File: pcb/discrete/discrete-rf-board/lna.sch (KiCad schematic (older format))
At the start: 7 parts, among them J701 Conn_Coaxial, J702 Conn_Coaxial, J703 Conn_Coaxial, J704 Conn_Coaxial, U701 SF2098H

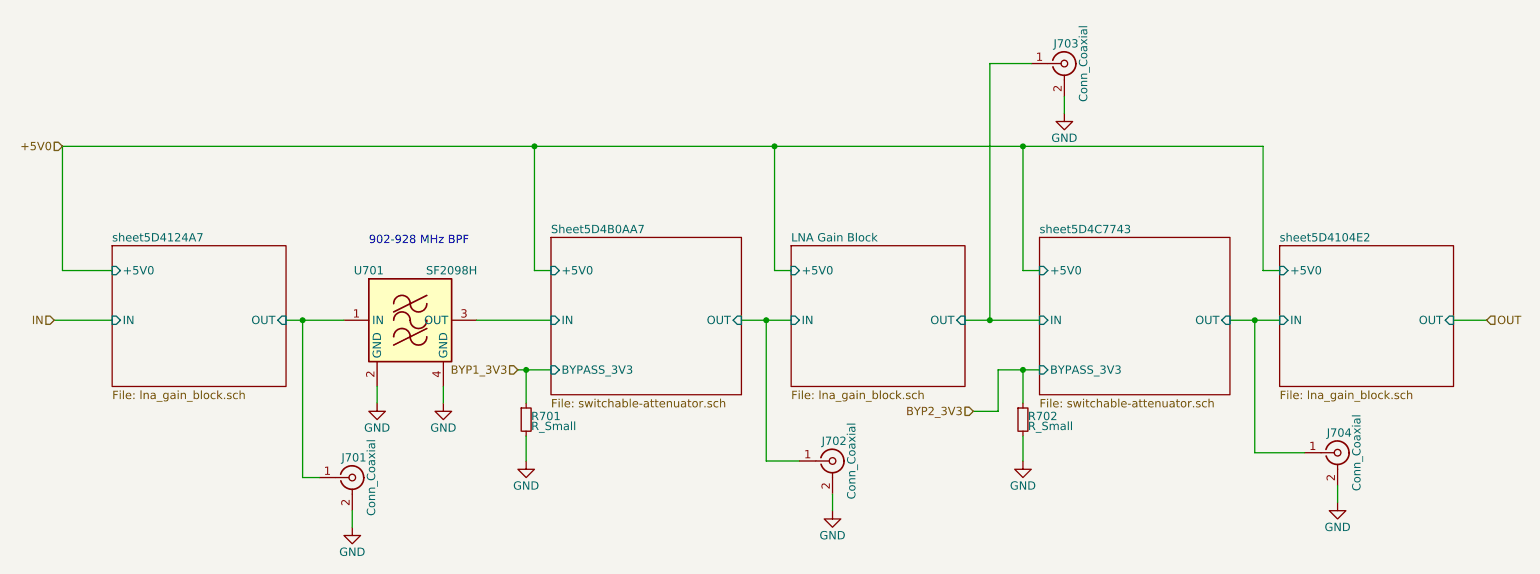
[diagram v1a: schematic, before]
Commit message: Wire out all control signals to connectors TODO PLL charge pump loop, bypass caps in attenuator circuit, antialiasing filter for ADC frontend
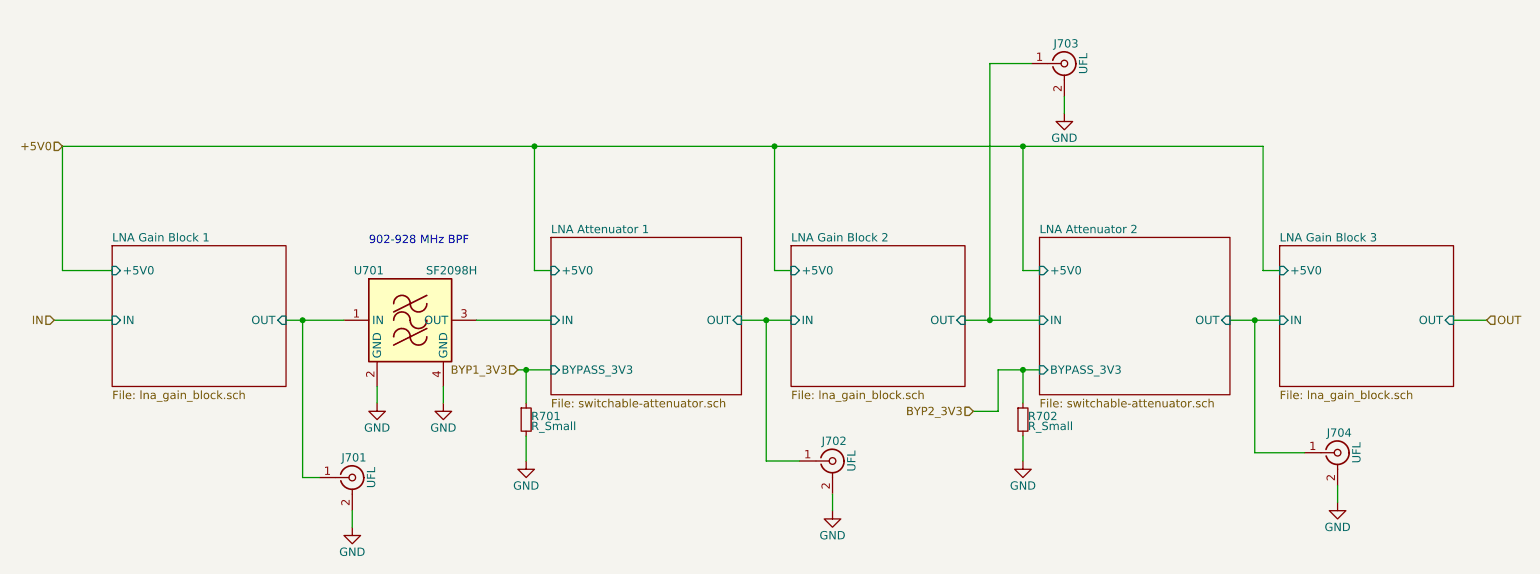
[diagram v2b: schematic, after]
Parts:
- J701, J702, J703, J704: value Conn_Coaxial -> UFL
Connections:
- net LNA Gain Block/IN renamed LNA Attenuator 1/OUT
- net LNA Gain Block/OUT renamed LNA Attenuator 2/IN
- net Sheet5D4B0AA7/IN renamed LNA Attenuator 1/IN
- net sheet5D4104E2/IN renamed LNA Attenuator 2/OUT
- net sheet5D4124A7/OUT renamed LNA Gain Block 1/OUT
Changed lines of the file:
@@
 $Descr A4 11693 8268
 encoding utf-8
-Sheet 6 19
+Sheet 13 19
 Title ""
 Date ""
@@
 S 5500 3200 1050 850
 U 5D3C8D48
-F0 "LNA Gain Block" 50
+F0 "LNA Gain Block 2" 50
 F1 "lna_gain_block.sch" 50
 F2 "IN" I L 5500 3650 50
@@
 S 8450 3200 1050 850
 U 5D4104E7
-F0 "sheet5D4104E2" 50
+F0 "LNA Gain Block 3" 50
 F1 "lna_gain_block.sch" 50
 F2 "IN" I L 8450 3650 50
@@
 S 1400 3200 1050 850
 U 5D4124AC
-F0 "sheet5D4124A7" 50
+F0 "LNA Gain Block 1" 50
 F1 "lna_gain_block.sch" 50
 F2 "IN" I L 1400 3650 50
@@
 S 4050 3150 1150 950
 U 5D4B0AA8
-F0 "Sheet5D4B0AA7" 50
+F0 "LNA Attenuator 1" 50
 F1 "switchable-attenuator.sch" 50
 F2 "OUT" I R 5200 3650 50
@@
 S 7000 3150 1150 950
 U 5D4C7749
-F0 "sheet5D4C7743" 50
+F0 "LNA Attenuator 2" 50
 F1 "switchable-attenuator.sch" 50
 F2 "OUT" I R 8150 3650 50
@@
 P 2850 4600
 F 0 "J701" H 2860 4720 50  0000 C CNN
-F 1 "Conn_Coaxial" V 2965 4600 50  0000 C CNN
+F 1 "UFL" V 2965 4600 50  0000 C CNN
 F 2 "" H 2850 4600 50  0001 C CNN
 F 3 " ~" H 2850 4600 50  0001 C CNN
@@
 P 5750 4500
 F 0 "J702" H 5760 4620 50  0000 C CNN
-F 1 "Conn_Coaxial" V 5865 4500 50  0000 C CNN
+F 1 "UFL" V 5865 4500 50  0000 C CNN
 F 2 "" H 5750 4500 50  0001 C CNN
 F 3 " ~" H 5750 4500 50  0001 C CNN
@@
 P 8800 4450
 F 0 "J704" H 8810 4570 50  0000 C CNN
-F 1 "Conn_Coaxial" V 8915 4450 50  0000 C CNN
+F 1 "UFL" V 8915 4450 50  0000 C CNN
 F 2 "" H 8800 4450 50  0001 C CNN
 F 3 " ~" H 8800 4450 50  0001 C CNN
@@
 P 7150 2100
 F 0 "J703" H 7160 2220 50  0000 C CNN
-F 1 "Conn_Coaxial" V 7265 2100 50  0000 C CNN
+F 1 "UFL" V 7265 2100 50  0000 C CNN
 F 2 "" H 7150 2100 50  0001 C CNN
 F 3 " ~" H 7150 2100 50  0001 C CNN

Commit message: Fix some parts
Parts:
- U701: footprint (none) -> discrete_footprints:Murata_SM2016-4; Mouser (none) -> 719-SF2098H
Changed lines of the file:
@@
 F 0 "U701" H 2950 3950 50  0000 C CNN
 F 1 "SF2098H" H 3450 3950 50  0000 C CNN
-F 2 "" H 3200 3200 50  0001 C CNN
+F 2 "discrete_footprints:Murata_SM2016-4" H 3200 3200 50  0001 C CNN
 F 3 "" H 3200 4050 50  0001 C CNN
+F 4 " 719-SF2098H " H 3200 3650 50  0001 C CNN "Mouser"
 	1    3200 3650
 	1    0    0    -1

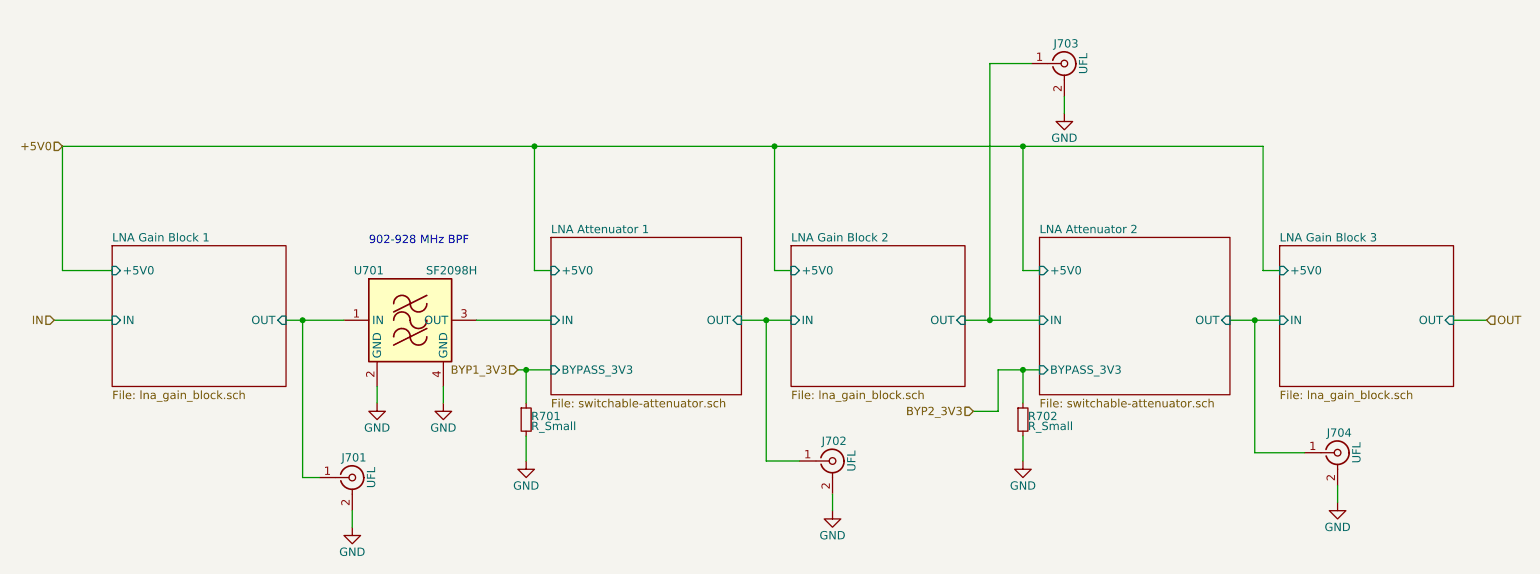
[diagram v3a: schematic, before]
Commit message: Add matching PNP/NPN transistor pairs, fix pin numbering for BFU520R transistors TODO fix biasing on power stage, source last NPN transistor, autofill and start sourcing passives
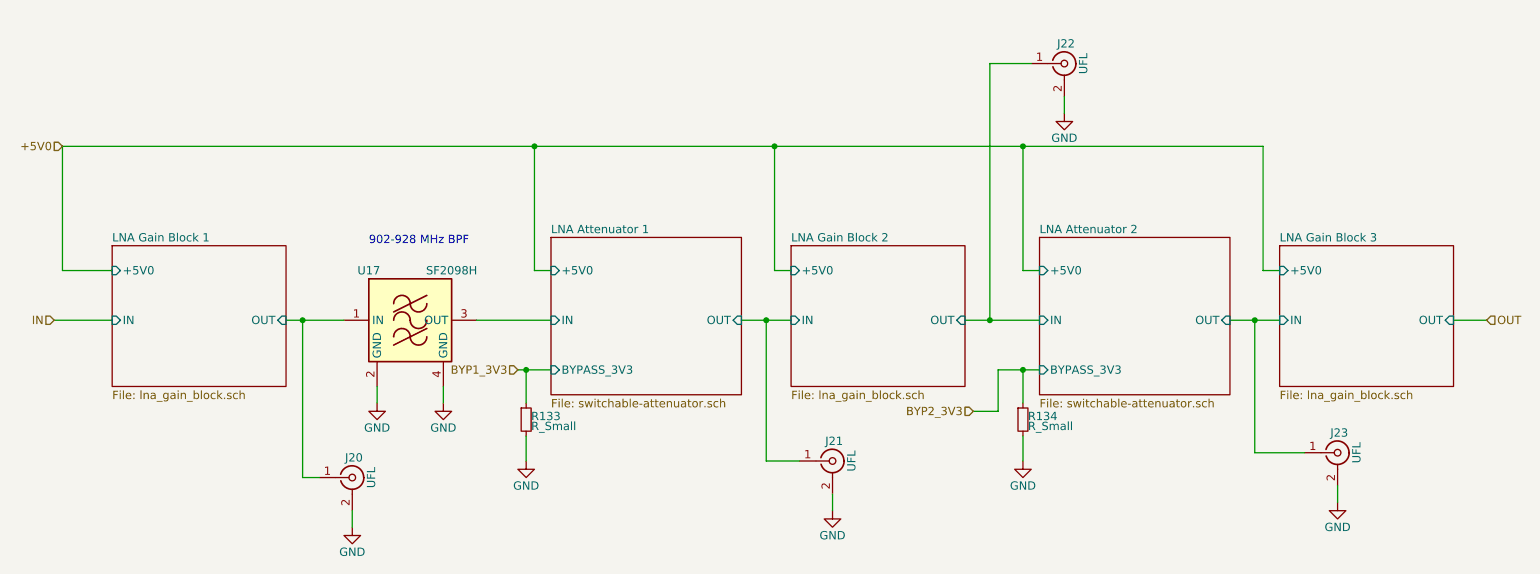
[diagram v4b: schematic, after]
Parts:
- renumbered J701 to J20, J702 to J21, J703 to J22, J704 to J23, R701 to R133, R702 to R134, U701 to U17
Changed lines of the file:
@@
 Connection ~ 6900 2600
 $Comp
-L discrete-parts:SF2098H U701
+L discrete-parts:SF2098H U17
 U 1 1 5D1AD426
 P 3200 3650
-F 0 "U701" H 2950 3950 50  0000 C CNN
+F 0 "U17" H 2950 3950 50  0000 C CNN
 F 1 "SF2098H" H 3450 3950 50  0000 C CNN
 F 2 "discrete_footprints:Murata_SM2016-4" H 3200 3200 50  0001 C CNN
@@
 	2450 3650 2550 3650
 $Comp
-L power:GND #PWR0702
+L power:GND #PWR0192
 U 1 1 5D1AE626
 P 3000 4150
-F 0 "#PWR0702" H 3000 3900 50  0001 C CNN
+F 0 "#PWR0192" H 3000 3900 50  0001 C CNN
 F 1 "GND" H 3000 4000 50  0000 C CNN
 F 2 "" H 3000 4150 50  0001 C CNN
@@
 $EndComp
 $Comp
-L power:GND #PWR0703
+L power:GND #PWR0193
 U 1 1 5D1AE8E4
 P 3400 4150
-F 0 "#PWR0703" H 3400 3900 50  0001 C CNN
+F 0 "#PWR0193" H 3400 3900 50  0001 C CNN
 F 1 "GND" H 3400 4000 50  0000 C CNN
 F 2 "" H 3400 4150 50  0001 C CNN
@@
 902-928 MHz BPF
 $Comp
-L Device:R_Small R701
+L Device:R_Small R133
 U 1 1 5D1B2D1C
 P 3900 4250
-F 0 "R701" H 3930 4270 50  0000 L CNN
+F 0 "R133" H 3930 4270 50  0000 L CNN
 F 1 "R_Small" H 3930 4210 50  0000 L CNN
 F 2 "" H 3900 4250 50  0001 C CNN
@@
 $EndComp
 $Comp
-L Device:R_Small R702
+L Device:R_Small R134
 U 1 1 5D1B32F5
 P 6900 4250
-F 0 "R702" H 6930 4270 50  0000 L CNN
+F 0 "R134" H 6930 4270 50  0000 L CNN
 F 1 "R_Small" H 6930 4210 50  0000 L CNN
 F 2 "" H 6900 4250 50  0001 C CNN
@@
 	3900 3950 4050 3950
 $Comp
-L power:GND #PWR0704
+L power:GND #PWR0194
 U 1 1 5D1B4BA9
 P 3900 4500
-F 0 "#PWR0704" H 3900 4250 50  0001 C CNN
+F 0 "#PWR0194" H 3900 4250 50  0001 C CNN
 F 1 "GND" H 3900 4350 50  0000 C CNN
 F 2 "" H 3900 4500 50  0001 C CNN
@@
 	6900 3950 7000 3950
 $Comp
-L power:GND #PWR0706
+L power:GND #PWR0196
 U 1 1 5D1B5E5F
 P 6900 4500
-F 0 "#PWR0706" H 6900 4250 50  0001 C CNN
+F 0 "#PWR0196" H 6900 4250 50  0001 C CNN
 F 1 "GND" H 6900 4350 50  0000 C CNN
 F 2 "" H 6900 4500 50  0001 C CNN
@@
 	6900 4500 6900 4350
 $Comp
-L Connector:Conn_Coaxial J701
+L Connector:Conn_Coaxial J20
 U 1 1 5D1BAD0A
 P 2850 4600
-F 0 "J701" H 2860 4720 50  0000 C CNN
+F 0 "J20" H 2860 4720 50  0000 C CNN
 F 1 "UFL" V 2965 4600 50  0000 C CNN
 F 2 "" H 2850 4600 50  0001 C CNN
@@
 $EndComp
 $Comp
-L Connector:Conn_Coaxial J702
+L Connector:Conn_Coaxial J21
 U 1 1 5D1BB7C4
 P 5750 4500
-F 0 "J702" H 5760 4620 50  0000 C CNN
+F 0 "J21" H 5760 4620 50  0000 C CNN
 F 1 "UFL" V 5865 4500 50  0000 C CNN
 F 2 "" H 5750 4500 50  0001 C CNN
@@
 $EndComp
 $Comp
-L Connector:Conn_Coaxial J704
+L Connector:Conn_Coaxial J23
 U 1 1 5D1BC003
 P 8800 4450
-F 0 "J704" H 8810 4570 50  0000 C CNN
+F 0 "J23" H 8810 4570 50  0000 C CNN
 F 1 "UFL" V 8915 4450 50  0000 C CNN
 F 2 "" H 8800 4450 50  0001 C CNN
@@
 $EndComp
 $Comp
-L Connector:Conn_Coaxial J703
+L Connector:Conn_Coaxial J22
 U 1 1 5D1BCC67
 P 7150 2100
-F 0 "J703" H 7160 2220 50  0000 C CNN
+F 0 "J22" H 7160 2220 50  0000 C CNN
 F 1 "UFL" V 7265 2100 50  0000 C CNN
 F 2 "" H 7150 2100 50  0001 C CNN
@@
 $EndComp
 $Comp
-L power:GND #PWR0707
+L power:GND #PWR0197
 U 1 1 5D1BD3CE
 P 7150 2400
-F 0 "#PWR0707" H 7150 2150 50  0001 C CNN
+F 0 "#PWR0197" H 7150 2150 50  0001 C CNN
 F 1 "GND" H 7150 2250 50  0000 C CNN
 F 2 "" H 7150 2400 50  0001 C CNN
@@
 $EndComp
 $Comp
-L power:GND #PWR0708
+L power:GND #PWR0198
 U 1 1 5D1BDEF3
 P 8800 4750
-F 0 "#PWR0708" H 8800 4500 50  0001 C CNN
+F 0 "#PWR0198" H 8800 4500 50  0001 C CNN
 F 1 "GND" H 8800 4600 50  0000 C CNN
 F 2 "" H 8800 4750 50  0001 C CNN
@@
 $EndComp
 $Comp
-L power:GND #PWR0705
+L power:GND #PWR0195
 U 1 1 5D1BE3A6
 P 5750 4800
-F 0 "#PWR0705" H 5750 4550 50  0001 C CNN
+F 0 "#PWR0195" H 5750 4550 50  0001 C CNN
 F 1 "GND" H 5750 4650 50  0000 C CNN
 F 2 "" H 5750 4800 50  0001 C CNN
@@
 $EndComp
 $Comp
-L power:GND #PWR0701
+L power:GND #PWR0191
 U 1 1 5D1BE863
 P 2850 4900
-F 0 "#PWR0701" H 2850 4650 50  0001 C CNN
+F 0 "#PWR0191" H 2850 4650 50  0001 C CNN
 F 1 "GND" H 2850 4750 50  0000 C CNN
 F 2 "" H 2850 4900 50  0001 C CNN

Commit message: Autofill all; TODO improve formatting on autofill_all output
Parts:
- J20, J21, J22, J23: footprint (none) -> discrete_footprints:2337019-1; Mouser (none) -> 571-2337019-1
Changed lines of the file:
@@
 F 0 "J20" H 2860 4720 50  0000 C CNN
 F 1 "UFL" V 2965 4600 50  0000 C CNN
-F 2 "" H 2850 4600 50  0001 C CNN
+F 2 "discrete_footprints:2337019-1" H 2850 4600 50  0001 C CNN
 F 3 " ~" H 2850 4600 50  0001 C CNN
+F 4 " 571-2337019-1" H 2850 4600 50  0001 C CNN "Mouser"
 	1    2850 4600
 	1    0    0    -1
@@
 F 0 "J21" H 5760 4620 50  0000 C CNN
 F 1 "UFL" V 5865 4500 50  0000 C CNN
-F 2 "" H 5750 4500 50  0001 C CNN
+F 2 "discrete_footprints:2337019-1" H 5750 4500 50  0001 C CNN
 F 3 " ~" H 5750 4500 50  0001 C CNN
+F 4 " 571-2337019-1" H 5750 4500 50  0001 C CNN "Mouser"
 	1    5750 4500
 	1    0    0    -1
@@
 F 0 "J23" H 8810 4570 50  0000 C CNN
 F 1 "UFL" V 8915 4450 50  0000 C CNN
-F 2 "" H 8800 4450 50  0001 C CNN
+F 2 "discrete_footprints:2337019-1" H 8800 4450 50  0001 C CNN
 F 3 " ~" H 8800 4450 50  0001 C CNN
+F 4 " 571-2337019-1" H 8800 4450 50  0001 C CNN "Mouser"
 	1    8800 4450
 	1    0    0    -1
@@
 F 0 "J22" H 7160 2220 50  0000 C CNN
 F 1 "UFL" V 7265 2100 50  0000 C CNN
-F 2 "" H 7150 2100 50  0001 C CNN
+F 2 "discrete_footprints:2337019-1" H 7150 2100 50  0001 C CNN
 F 3 " ~" H 7150 2100 50  0001 C CNN
+F 4 " 571-2337019-1" H 7150 2100 50  0001 C CNN "Mouser"
 	1    7150 2100
 	1    0    0    -1

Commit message: Footprint some stuff
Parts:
- R133, R134: value R_Small -> 10kR
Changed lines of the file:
@@
 P 3900 4250
 F 0 "R133" H 3930 4270 50  0000 L CNN
-F 1 "R_Small" H 3930 4210 50  0000 L CNN
+F 1 "10kR" H 3930 4210 50  0000 L CNN
 F 2 "" H 3900 4250 50  0001 C CNN
 F 3 "~" H 3900 4250 50  0001 C CNN
@@
 P 6900 4250
 F 0 "R134" H 6930 4270 50  0000 L CNN
-F 1 "R_Small" H 6930 4210 50  0000 L CNN
+F 1 "10kR" H 6930 4210 50  0000 L CNN
 F 2 "" H 6900 4250 50  0001 C CNN
 F 3 "~" H 6900 4250 50  0001 C CNN

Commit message: Autofill
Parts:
- R133, R134: footprint (none) -> Resistor_SMD:R_0402_1005Metric; Mouser (none) -> 603-AC0402FR-1310KL
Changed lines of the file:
@@
 F 0 "R133" H 3930 4270 50  0000 L CNN
 F 1 "10kR" H 3930 4210 50  0000 L CNN
-F 2 "" H 3900 4250 50  0001 C CNN
+F 2 "Resistor_SMD:R_0402_1005Metric" H 3900 4250 50  0001 C CNN
 F 3 "~" H 3900 4250 50  0001 C CNN
+F 4 "603-AC0402FR-1310KL" H 3900 4250 50  0001 C CNN "Mouser"
 	1    3900 4250
 	1    0    0    -1
@@
 F 0 "R134" H 6930 4270 50  0000 L CNN
 F 1 "10kR" H 6930 4210 50  0000 L CNN
-F 2 "" H 6900 4250 50  0001 C CNN
+F 2 "Resistor_SMD:R_0402_1005Metric" H 6900 4250 50  0001 C CNN
 F 3 "~" H 6900 4250 50  0001 C CNN
+F 4 "603-AC0402FR-1310KL" H 6900 4250 50  0001 C CNN "Mouser"
 	1    6900 4250
 	1    0    0    -1

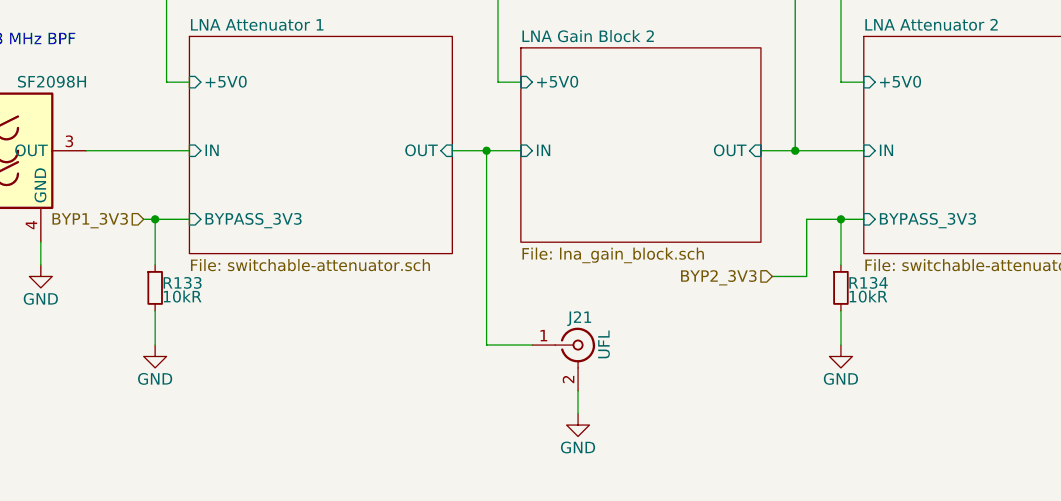
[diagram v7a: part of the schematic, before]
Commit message: Reannotate everything; I'm trying to cut down the number of components
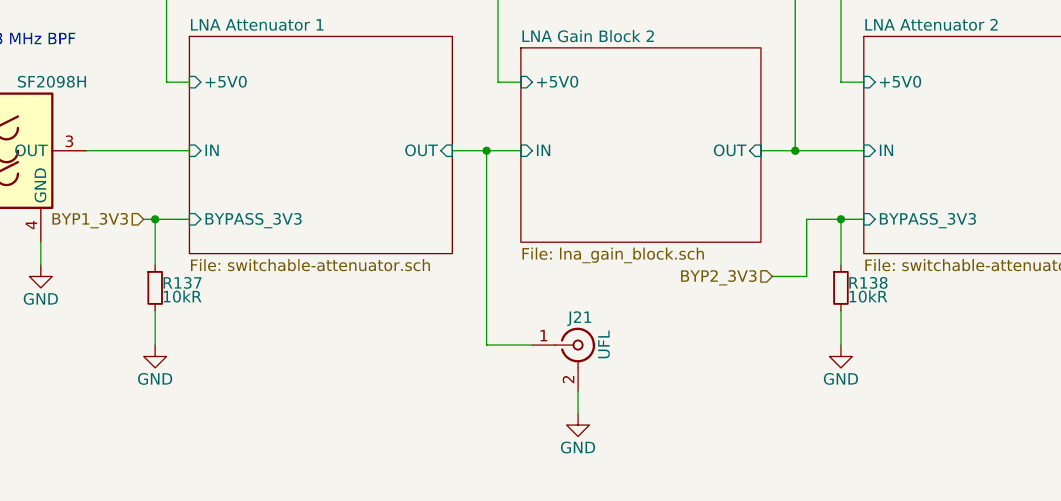
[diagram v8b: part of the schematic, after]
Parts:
- renumbered R133 to R137, R134 to R138
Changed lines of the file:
@@
 	2450 3650 2550 3650
 $Comp
-L power:GND #PWR0192
+L power:GND #PWR0189
 U 1 1 5D1AE626
 P 3000 4150
-F 0 "#PWR0192" H 3000 3900 50  0001 C CNN
+F 0 "#PWR0189" H 3000 3900 50  0001 C CNN
 F 1 "GND" H 3000 4000 50  0000 C CNN
 F 2 "" H 3000 4150 50  0001 C CNN
@@
 $EndComp
 $Comp
-L power:GND #PWR0193
+L power:GND #PWR0190
 U 1 1 5D1AE8E4
 P 3400 4150
-F 0 "#PWR0193" H 3400 3900 50  0001 C CNN
+F 0 "#PWR0190" H 3400 3900 50  0001 C CNN
 F 1 "GND" H 3400 4000 50  0000 C CNN
 F 2 "" H 3400 4150 50  0001 C CNN
@@
 902-928 MHz BPF
 $Comp
-L Device:R_Small R133
+L Device:R_Small R137
 U 1 1 5D1B2D1C
 P 3900 4250
-F 0 "R133" H 3930 4270 50  0000 L CNN
+F 0 "R137" H 3930 4270 50  0000 L CNN
 F 1 "10kR" H 3930 4210 50  0000 L CNN
 F 2 "Resistor_SMD:R_0402_1005Metric" H 3900 4250 50  0001 C CNN
@@
 $EndComp
 $Comp
-L Device:R_Small R134
+L Device:R_Small R138
 U 1 1 5D1B32F5
 P 6900 4250
-F 0 "R134" H 6930 4270 50  0000 L CNN
+F 0 "R138" H 6930 4270 50  0000 L CNN
 F 1 "10kR" H 6930 4210 50  0000 L CNN
 F 2 "Resistor_SMD:R_0402_1005Metric" H 6900 4250 50  0001 C CNN
@@
 	3900 3950 4050 3950
 $Comp
-L power:GND #PWR0194
+L power:GND #PWR0191
 U 1 1 5D1B4BA9
 P 3900 4500
-F 0 "#PWR0194" H 3900 4250 50  0001 C CNN
+F 0 "#PWR0191" H 3900 4250 50  0001 C CNN
 F 1 "GND" H 3900 4350 50  0000 C CNN
 F 2 "" H 3900 4500 50  0001 C CNN
@@
 	6900 3950 7000 3950
 $Comp
-L power:GND #PWR0196
+L power:GND #PWR0193
 U 1 1 5D1B5E5F
 P 6900 4500
-F 0 "#PWR0196" H 6900 4250 50  0001 C CNN
+F 0 "#PWR0193" H 6900 4250 50  0001 C CNN
 F 1 "GND" H 6900 4350 50  0000 C CNN
 F 2 "" H 6900 4500 50  0001 C CNN
@@
 $EndComp
 $Comp
-L power:GND #PWR0197
+L power:GND #PWR0194
 U 1 1 5D1BD3CE
 P 7150 2400
-F 0 "#PWR0197" H 7150 2150 50  0001 C CNN
+F 0 "#PWR0194" H 7150 2150 50  0001 C CNN
 F 1 "GND" H 7150 2250 50  0000 C CNN
 F 2 "" H 7150 2400 50  0001 C CNN
@@
 $EndComp
 $Comp
-L power:GND #PWR0198
+L power:GND #PWR0195
 U 1 1 5D1BDEF3
 P 8800 4750
-F 0 "#PWR0198" H 8800 4500 50  0001 C CNN
+F 0 "#PWR0195" H 8800 4500 50  0001 C CNN
 F 1 "GND" H 8800 4600 50  0000 C CNN
 F 2 "" H 8800 4750 50  0001 C CNN
@@
 $EndComp
 $Comp
-L power:GND #PWR0195
+L power:GND #PWR0192
 U 1 1 5D1BE3A6
 P 5750 4800
-F 0 "#PWR0195" H 5750 4550 50  0001 C CNN
+F 0 "#PWR0192" H 5750 4550 50  0001 C CNN
 F 1 "GND" H 5750 4650 50  0000 C CNN
 F 2 "" H 5750 4800 50  0001 C CNN
@@
 $EndComp
 $Comp
-L power:GND #PWR0191
+L power:GND #PWR0188
 U 1 1 5D1BE863
 P 2850 4900
-F 0 "#PWR0191" H 2850 4650 50  0001 C CNN
+F 0 "#PWR0188" H 2850 4650 50  0001 C CNN
 F 1 "GND" H 2850 4750 50  0000 C CNN
 F 2 "" H 2850 4900 50  0001 C CNN
